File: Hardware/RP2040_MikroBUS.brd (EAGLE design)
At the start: 30.5 x 94 mm, 161 parts, among them J1 SWD, J3 Qwiic, J5 USB C, J6 microSD, J9 MIKROBUS_SMD_BLACK1, Q1 20V/4.2A/52mΩ/1.4W, U2 MAX17048, U3 MCP73831, U4 W25QXX128MBIT, U5 RP2040, U7 3.3V, Y2 12MHz

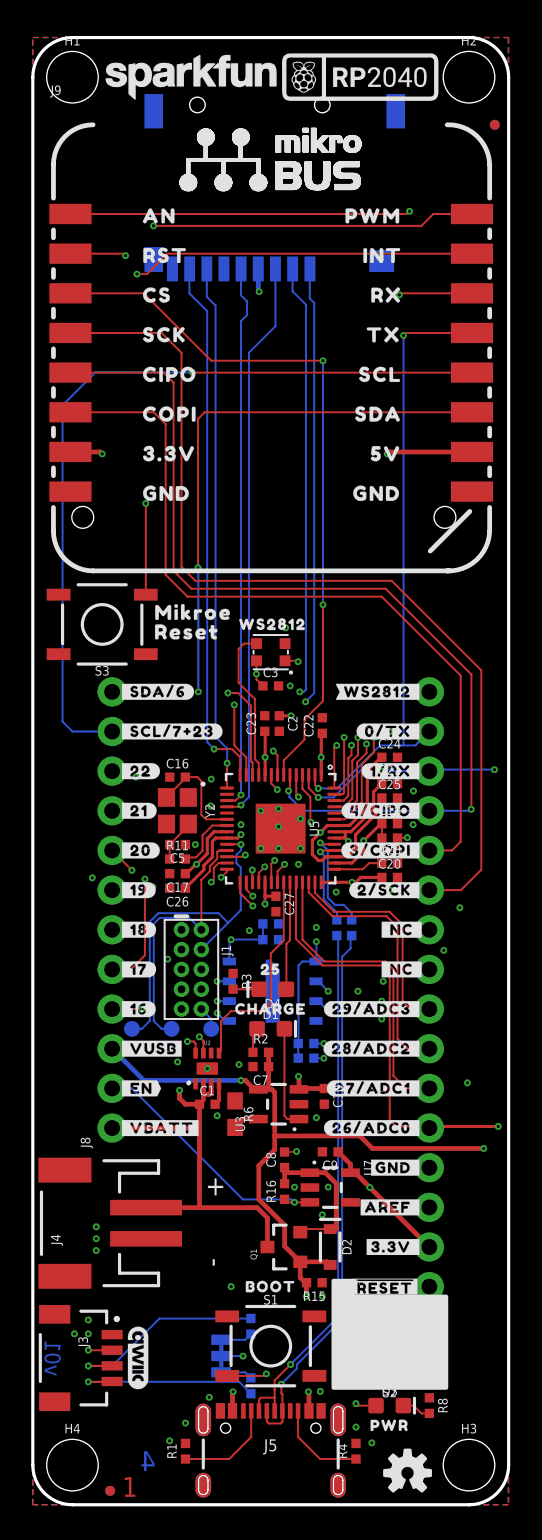
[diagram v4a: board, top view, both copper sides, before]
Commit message: Design review before ordering changes
* Add a pullup and NC jumper on the CS line
* A jumper on the PWR LED
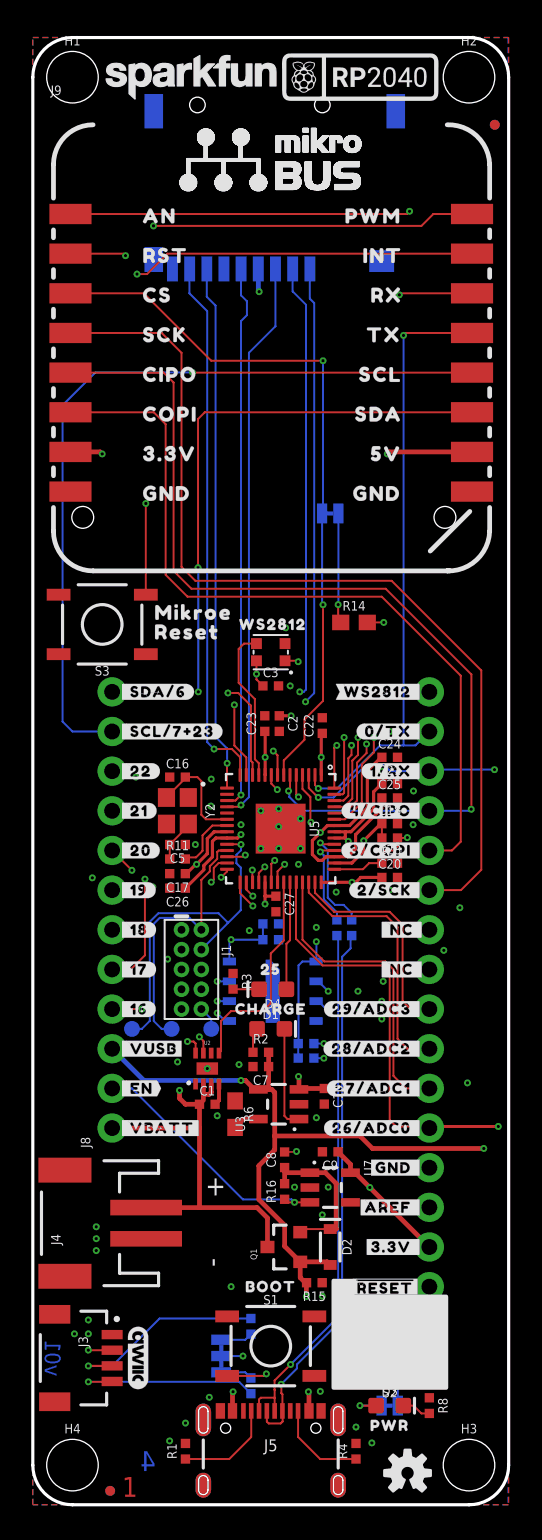
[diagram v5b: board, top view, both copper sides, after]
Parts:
- added !CS!, PWR: JUMPER-SMT_2_NC_TRACE_SILK, SparkFun-Jumpers:SMT-JUMPER_2_NC_TRACE_SILK
- added R14: 100k, SparkFun-Resistors:0603
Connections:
- new net N$10: D3.A, PWR.1
- new net N$8: !CS!.2, R14.1
- net !SPI0_CS!: now also !CS!.1
- net 3.3V: now also PWR.2, R14.2; no longer D3.A
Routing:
- net N$8: track 0.00 -> 7.06 mm, vias 0 -> 1
- net N$10: track 0.00 -> 2.41 mm, vias 0 -> 1
- net 3.3V: track 52.7 -> 53.7 mm, vias 18 -> 19
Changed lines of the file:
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@@
 <?xml version="1.0" encoding="utf-8"?>
 <!DOCTYPE eagle SYSTEM "eagle.dtd">
-<eagle version="9.4.2">
+<eagle version="9.5.2">
 <drawing>
 <settings>
@@
 <layer number="27" name="tValues" color="7" fill="1" visible="no" active="yes"/>
 <layer number="28" name="bValues" color="7" fill="1" visible="no" active="yes"/>
-<layer number="29" name="tStop" color="7" fill="3" visible="no" active="yes"/>
+<layer number="29" name="tStop" color="7" fill="3" visible="yes" active="yes"/>
 <layer number="30" name="bStop" color="7" fill="6" visible="no" active="yes"/>
 <layer number="31" name="tCream" color="7" fill="4" visible="no" active="yes"/>
@@
 <layer number="95" name="Names" color="7" fill="1" visible="no" active="no"/>
 <layer number="96" name="Values" color="7" fill="1" visible="no" active="no"/>
-<layer number="2" name="gndvert" color="10" fill="7" visible="no" active="yes"/>
-<layer number="15" name="pwrhorz" color="4" fill="7" visible="no" active="yes"/>
+<layer number="2" name="gndvert" color="10" fill="7" visible="yes" active="yes"/>
+<layer number="15" name="pwrhorz" color="4" fill="7" visible="yes" active="yes"/>
 <layer number="3" name="Route3" color="4" fill="3" visible="no" active="no"/>
 <layer number="4" name="Route4" color="1" fill="4" visible="no" active="no"/>
@@
 &lt;li&gt;4mil Annular Rings&lt;/li&gt;
 &lt;li&gt;0.2mm/7.9mil Vias&lt;/li&gt;
+&lt;li&gt;2.5mil Stop Mask&lt;/li&gt;
 &lt;/ul&gt;</description>
 <param name="layerSetup" value="(1+2*15+16)"/>
@@
 <param name="mvStopFrame" value="1"/>
 <param name="mvCreamFrame" value="0"/>
-<param name="mlMinStopFrame" value="4mil"/>
-<param name="mlMaxStopFrame" value="4mil"/>
+<param name="mlMinStopFrame" value="2.5mil"/>
+<param name="mlMaxStopFrame" value="2.5mil"/>
 <param name="mlMinCreamFrame" value="0mil"/>
 <param name="mlMaxCreamFrame" value="0mil"/>
 <param name="mlViaStopLimit" value="25mil"/>
 <param name="srRoundness" value="0"/>
-<param name="srMinRoundness" value="0mil"/>
-<param name="srMaxRoundness" value="0mil"/>
+<param name="srMinRoundness" value="2mil"/>
+<param name="srMaxRoundness" value="2mil"/>
 <param name="slThermalIsolate" value="10mil"/>
 <param name="slThermalsForVias" value="0"/>
@@
 <element name="U$84" library="output" package="INT0" value="" x="20.447" y="80.01" smashed="yes"/>
 <element name="U$85" library="output" package="PWM0" value="" x="19.304" y="82.55" smashed="yes"/>
+<element name="!CS!" library="SparkFun-Jumpers" package="SMT-JUMPER_2_NC_TRACE_SILK" package3d_urn="urn:adsk.eagle:package:39281/1" value="JUMPER-SMT_2_NC_TRACE_SILK" x="19.05" y="63.5" smashed="yes" rot="MR180">
+<attribute name="NAME" x="19.05" y="62.357" size="0.6096" layer="26" font="vector" ratio="20" rot="MR180" align="bottom-center"/>
+<attribute name="VALUE" x="19.05" y="64.643" size="0.6096" layer="28" font="vector" ratio="20" rot="MR180" align="top-center"/>
+</element>
+<element name="R14" library="SparkFun-Resistors" package="0603" value="100k" x="20.574" y="56.515" smashed="yes">
+<attribute name="NAME" x="20.574" y="57.277" size="0.6096" layer="25" font="vector" ratio="20" align="bottom-center"/>
+<attribute name="PROD_ID" value="RES-07828" x="20.574" y="56.515" size="1.778" layer="27" font="vector" ratio="15" display="off"/>
+<attribute name="VALUE" x="20.574" y="55.753" size="0.6096" layer="27" font="vector" ratio="20" align="top-center"/>
+</element>
+<element name="PWR" library="SparkFun-Jumpers" package="SMT-JUMPER_2_NC_TRACE_SILK" package3d_urn="urn:adsk.eagle:package:39281/1" value="JUMPER-SMT_2_NC_TRACE_SILK" x="22.86" y="6.35" smashed="yes" rot="MR180">
+<attribute name="NAME" x="22.86" y="5.207" size="0.6096" layer="26" font="vector" ratio="20" rot="MR180" align="bottom-center"/>
+<attribute name="VALUE" x="22.86" y="7.493" size="0.6096" layer="28" font="vector" ratio="20" rot="MR180" align="top-center"/>
+</element>
 </elements>
 <signals>
@@
 <wire x1="20.0152" y1="42.7257" x2="20.0152" y2="43.107" width="0.2032" layer="1"/>
 <wire x1="18.0006" y1="29.5402" x2="18.6436" y2="29.5402" width="0.127" layer="16"/>
-<contactref element="D3" pad="A"/>
-<wire x1="21.983" y1="6.35" x2="20.828" y2="6.35" width="0.127" layer="1"/>
-<wire x1="20.828" y1="6.35" x2="20.701" y2="6.477" width="0.127" layer="1"/>
-<via x="20.701" y="6.477" extent="1-16" drill="0.2" diameter="0.45"/>
 <wire x1="15.5702" y1="38.981" x2="14.875" y2="38.981" width="0.2032" layer="1"/>
 <contactref element="J9" pad="7"/>
@@
 <via x="14.5" y="77.7" extent="1-16" drill="0.2" diameter="0.45"/>
 <contactref element="D5" pad="VCC"/>
+<contactref element="R14" pad="2"/>
+<contactref element="PWR" pad="2"/>
+<wire x1="23.3807" y1="6.35" x2="23.3807" y2="7.62" width="0.127" layer="16"/>
+<via x="23.3807" y="7.62" extent="1-16" drill="0.2" diameter="0.45"/>
+<wire x1="21.424" y1="56.515" x2="22.479" y2="56.515" width="0.127" layer="1"/>
+<via x="22.479" y="56.515" extent="1-16" drill="0.2" diameter="0.45"/>
 </signal>
 <signal name="GND">
@@
 <wire x1="16.075" y1="46.7435" x2="16.075" y2="47.675" width="0.127" layer="1"/>
 <via x="18.588" y="57.6489" extent="1-16" drill="0.2" diameter="0.45"/>
-<wire x1="18.588" y1="73.279" x2="18.588" y2="57.6489" width="0.127" layer="16"/>
 <via x="18.588" y="73.279" extent="1-16" drill="0.2" diameter="0.45"/>
 <wire x1="18.588" y1="73.279" x2="11.43" y2="73.279" width="0.127" layer="1"/>
@@
 <wire x1="17.4" y1="50.3" x2="17.4" y2="49" width="0.127" layer="1"/>
 <wire x1="17.4" y1="49" x2="16.075" y2="47.675" width="0.127" layer="1"/>
+<contactref element="!CS!" pad="1"/>
+<wire x1="18.588" y1="73.279" x2="18.588" y2="63.5587" width="0.127" layer="16"/>
+<wire x1="18.588" y1="63.5587" x2="18.5293" y2="63.5" width="0.127" layer="16"/>
+<wire x1="18.5293" y1="63.5" x2="18.5293" y2="57.7076" width="0.127" layer="16"/>
+<wire x1="18.5293" y1="57.7076" x2="18.588" y2="57.6489" width="0.127" layer="16"/>
+</signal>
+<signal name="N$8">
+<contactref element="!CS!" pad="2"/>
+<contactref element="R14" pad="1"/>
+<wire x1="19.5707" y1="63.5" x2="19.5707" y2="57.6707" width="0.127" layer="16"/>
+<wire x1="19.5707" y1="57.6707" x2="19.558" y2="57.658" width="0.127" layer="16"/>
+<via x="19.558" y="57.658" extent="1-16" drill="0.2" diameter="0.45"/>
+<wire x1="19.724" y1="56.515" x2="19.558" y2="56.681" width="0.127" layer="1"/>
+<wire x1="19.558" y1="56.681" x2="19.558" y2="57.658" width="0.127" layer="1"/>
+</signal>
+<signal name="N$10">
+<contactref element="D3" pad="A"/>
+<contactref element="PWR" pad="1"/>
+<wire x1="21.983" y1="6.35" x2="20.955" y2="6.35" width="0.127" layer="1"/>
+<via x="20.955" y="6.35" extent="1-16" drill="0.2" diameter="0.45"/>
+<wire x1="20.955" y1="6.35" x2="22.3393" y2="6.35" width="0.127" layer="16"/>
 </signal>
 </signals>

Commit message: Update silk screen labels and generate gerbers
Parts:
- added U$86: (no value), output:#CS_PU#0
- added U$87: (no value), output:#PWR#0
- added U$88: (no value), output:MIKROBUS0
- moved U$17 54.7 mm to (15.4, 69.8)
- moved U$32 54.3 mm to (15.4, 73.2)
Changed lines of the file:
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@@
 <?xml version="1.0" encoding="utf-8"?>
 <!DOCTYPE eagle SYSTEM "eagle.dtd">
-<eagle version="9.5.2">
+<eagle version="9.6.2">
 <drawing>
 <settings>
@@
 <element name="U$28" library="output" package="##RESET##0" value="" x="24.892" y="13.97" smashed="yes"/>
 <element name="U$64" library="SparkFun-Aesthetics" package="QWIIC_4MM" value="" x="6.731" y="9.398" smashed="yes" rot="R270"/>
-<element name="U$32" library="SparkFun-Aesthetics" package="SFE_LOGO_NAME_FLAME_.1" value="" x="12.827" y="18.923" smashed="yes" rot="MR0"/>
+<element name="U$32" library="SparkFun-Aesthetics" package="SFE_LOGO_NAME_FLAME_.1" value="" x="15.367" y="73.152" smashed="yes" rot="MR0"/>
 <element name="U$54" library="output" package="250" value="" x="15.24" y="34.29" smashed="yes"/>
 <element name="U$55" library="output" package="CHARGE0" value="" x="15.24" y="31.75" smashed="yes"/>
@@
 <element name="U$71" library="output" package="#_WS2812#0" value="" x="25.019" y="52.07" smashed="yes" rot="MR0"/>
 <element name="U$72" library="output" package="#I2C#0" value="" x="10.033" y="7.62" smashed="yes" rot="MR90"/>
-<element name="U$17" library="SparkFun-Aesthetics" package="RASPI_RP2040_LOGO_10MM" value="RASPI_RP2040_LOGO_10MM" x="12.7" y="15.24" smashed="yes" rot="MR0"/>
+<element name="U$17" library="SparkFun-Aesthetics" package="RASPI_RP2040_LOGO_10MM" value="RASPI_RP2040_LOGO_10MM" x="15.367" y="69.85" smashed="yes" rot="MR0"/>
 <element name="U$73" library="SparkFun-Aesthetics" package="RASPI_RP2040_LOGO_10MM" value="RASPI_RP2040_LOGO_10MM" x="20.955" y="91.44" smashed="yes"/>
 <element name="U$30" library="output" package="WS28120" value="" x="12.7" y="56.388" smashed="yes"/>
@@
 <attribute name="VALUE" x="22.86" y="7.493" size="0.6096" layer="28" font="vector" ratio="20" rot="MR180" align="top-center"/>
 </element>
+<element name="U$86" library="output" package="#CS_PU#0" value="" x="18.161" y="63.5" smashed="yes" rot="MR0"/>
+<element name="U$87" library="output" package="#PWR#0" value="" x="28.448" y="6.35" smashed="yes" rot="MR0"/>
+<element name="U$88" library="output" package="MIKROBUS0" value="" x="22.352" y="67.056" smashed="yes" rot="MR0"/>
 </elements>
 <signals>

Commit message: Update labels
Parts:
- removed !CS!: JUMPER-SMT_2_NC_TRACE_SILK, SparkFun-Jumpers:SMT-JUMPER_2_NC_TRACE_SILK
- removed R14: 100k, SparkFun-Resistors:0603
- removed S3: MOMENTARY-SWITCH-SPST-SMD-5.2MM-TALL, SparkFun-Switches:TACTILE_SWITCH_SMD_5.2MM
- moved U$83 5.99 mm to (15.9, 74.3)
- moved U$84 5.95 mm to (15.9, 76.2)
- moved U$29 5.85 mm to (10.2, 78.1)
- moved U$85 5.61 mm to (15.9, 78.1)
- moved U$82 5.45 mm to (15.9, 72.4)
- moved U$44 5.39 mm to (10.2, 76.2)
- moved U$79 5.12 mm to (15.9, 66.7)
- moved U$45 5.04 mm to (10.2, 74.2)
- moved U$81 4.72 mm to (15.9, 70.5)
- moved U$74 4.58 mm to (10.2, 72.4)
- moved U$60 4.26 mm to (10.2, 70.5)
- moved U$80 4.26 mm to (15.9, 68.6)
- moved U$75 4.02 mm to (10.2, 68.6)
- moved U$78 3.94 mm to (15.9, 64.8)
- moved U$76 3.84 mm to (10.2, 66.8)
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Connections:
- removed net N$8: !CS!.2, R14.1
- net !SPI0_CS!: no longer !CS!.1
- net 3.3V: no longer R14.2
- net GND: no longer S3.1
- net MIK_RST: no longer S3.3
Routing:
- net N$8: track 7.06 -> 0.00 mm, vias 1 -> 0
- net !SPI0_CS!: track 45.6 -> 39.7 mm
- net MIK_RST: track 26.3 -> 20.4 mm
- net 3.3V: track 53.7 -> 52.6 mm, vias 19 -> 18

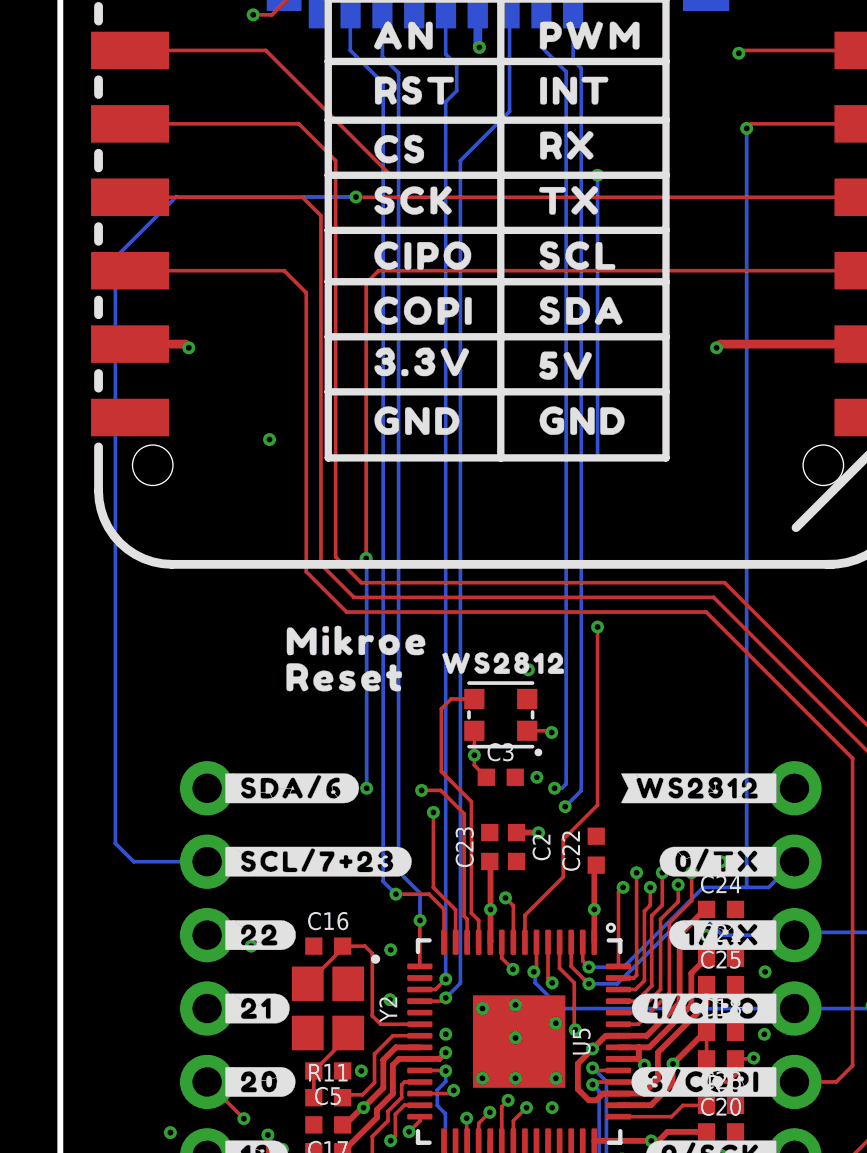
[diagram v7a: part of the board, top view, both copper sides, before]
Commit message: From mikroE convo
* Remove reset button
* Remove CS pullup
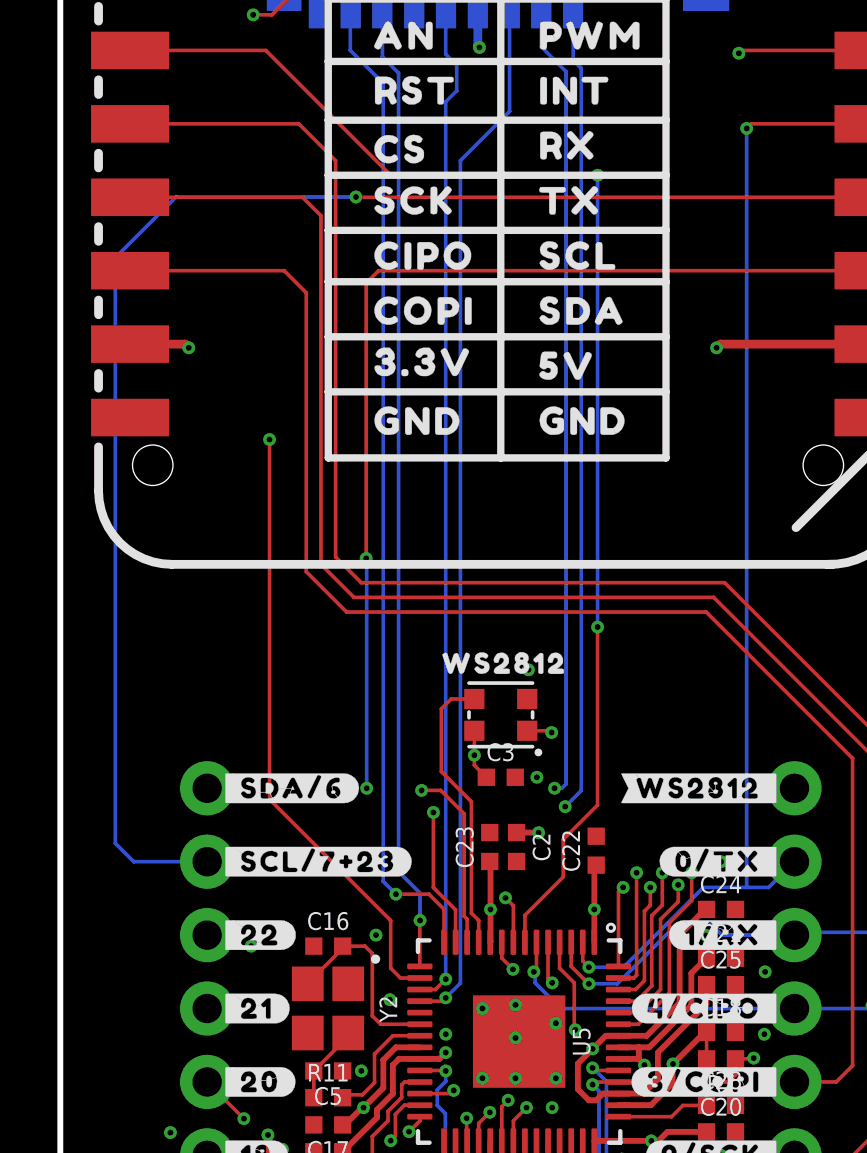
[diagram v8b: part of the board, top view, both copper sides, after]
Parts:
- removed U$43: (no value), output:MIKROE0
- removed U$46: (no value), output:RESET0
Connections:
- removed net MIK_RST: J9.2
- new net GPIO13: J9.2, U5.16
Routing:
- net GPIO13: track 0.00 -> 41.6 mm, vias 0 -> 2
- net MIK_RST: track 20.4 -> 0.00 mm, vias 2 -> 0
- net !SPI0_CS!: track 39.7 -> 45.5 mm
